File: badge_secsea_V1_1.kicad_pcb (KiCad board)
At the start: 4 copper layers, 74.1 x 130 mm, 132 parts, among them J1 USB_C_Receptacle_USB2.0_14P, J2 PM254-2-06-S-8.5, J3 PM254-2-06-S-8.5, J4 AFC07-S24ECA-00, J5 Micro_SD_Card_Det1, Q1 2N7002, Q2 SI1308EDL, Q3 SI2301, SW1 TS-1187A-B-A-B, SW2 K2-1112SW-A4SW-04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

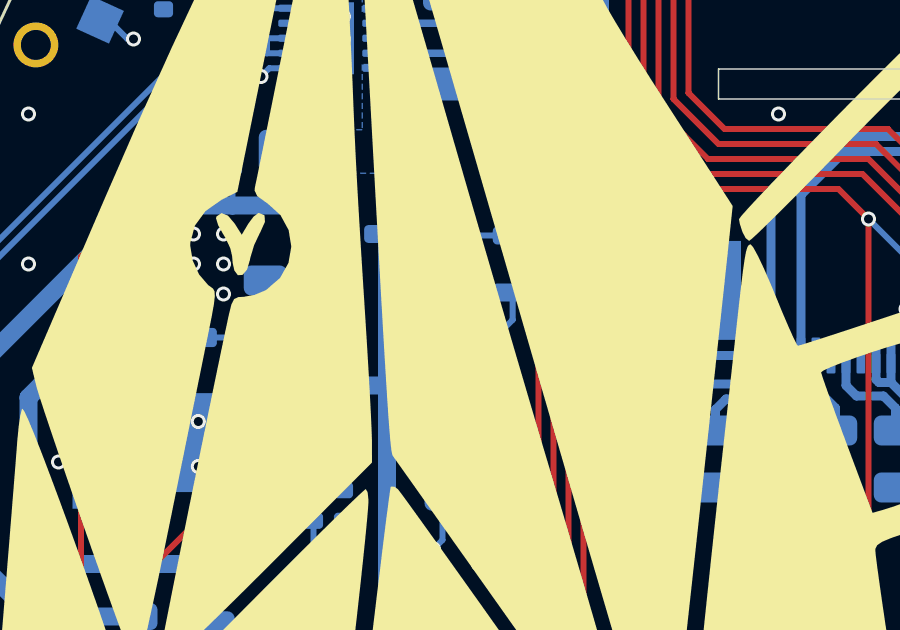
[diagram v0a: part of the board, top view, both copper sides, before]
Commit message: Consumption fix: Op amp now connected to +3.3V instead of VBat (Schematic + PCB)
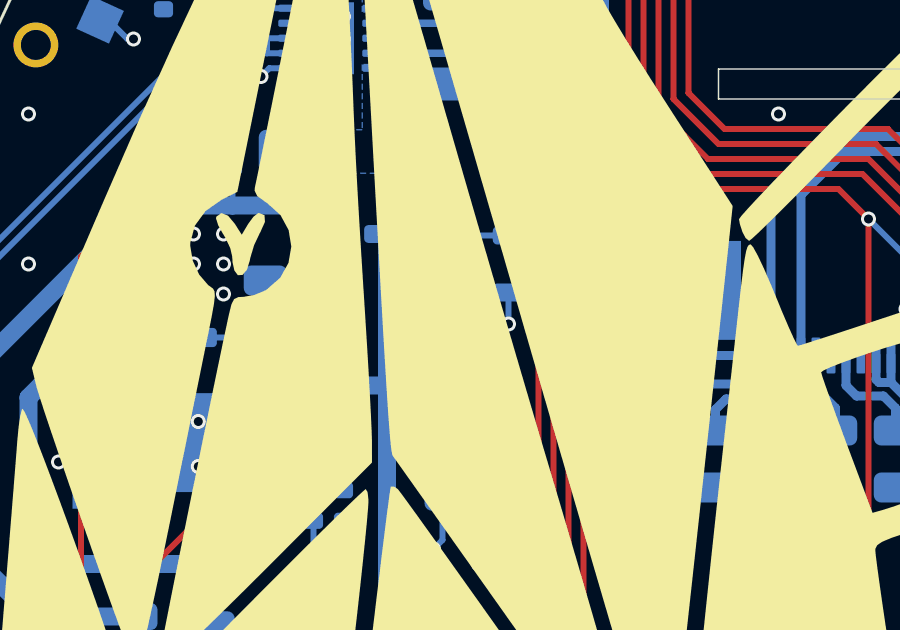
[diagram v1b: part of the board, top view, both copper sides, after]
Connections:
- U7 pad 5: Net-(Q3-D) -> +3.3V
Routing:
- net +3.3V: track 531.5 -> 538.0 mm, vias 38 -> 39
- net Net-(Q3-D): track 47.9 -> 42.6 mm

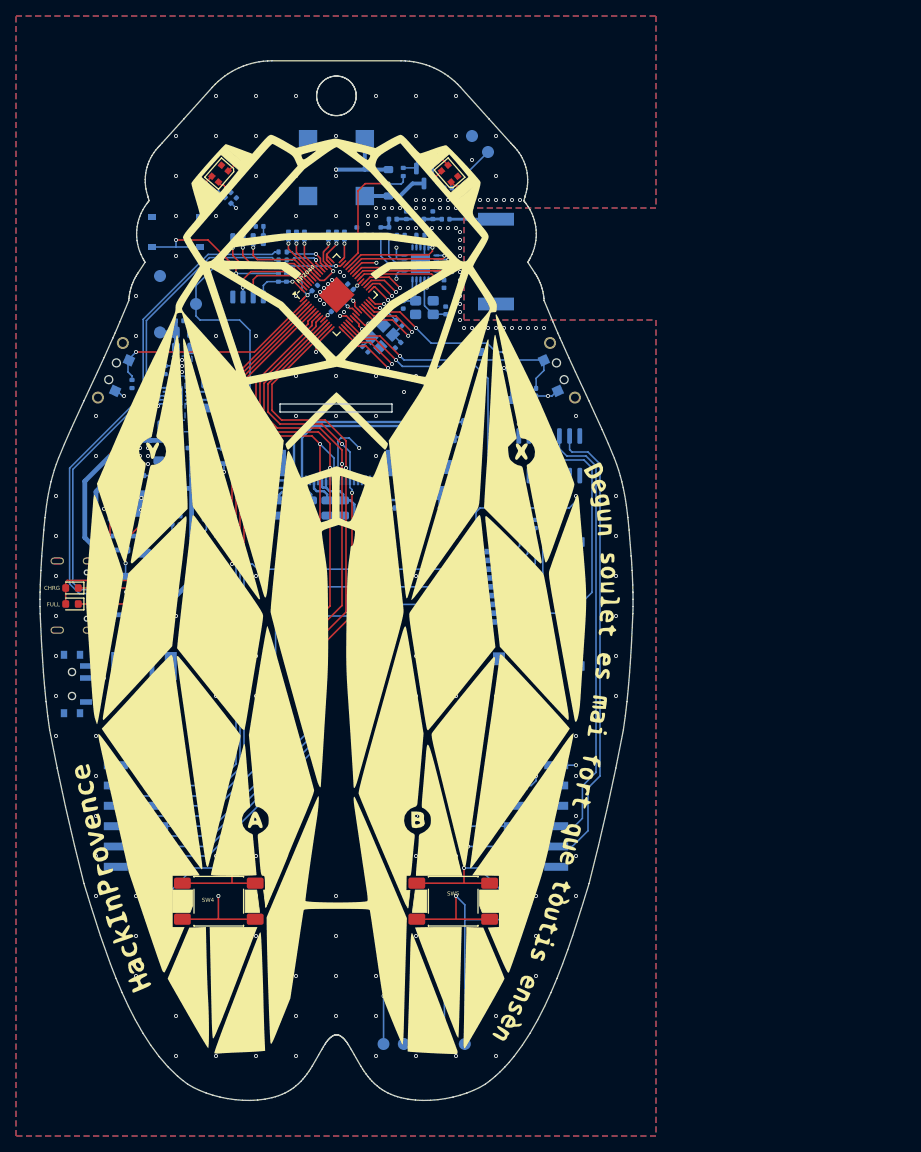
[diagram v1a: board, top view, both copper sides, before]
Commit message: Working on new antenna keepout zone and position.
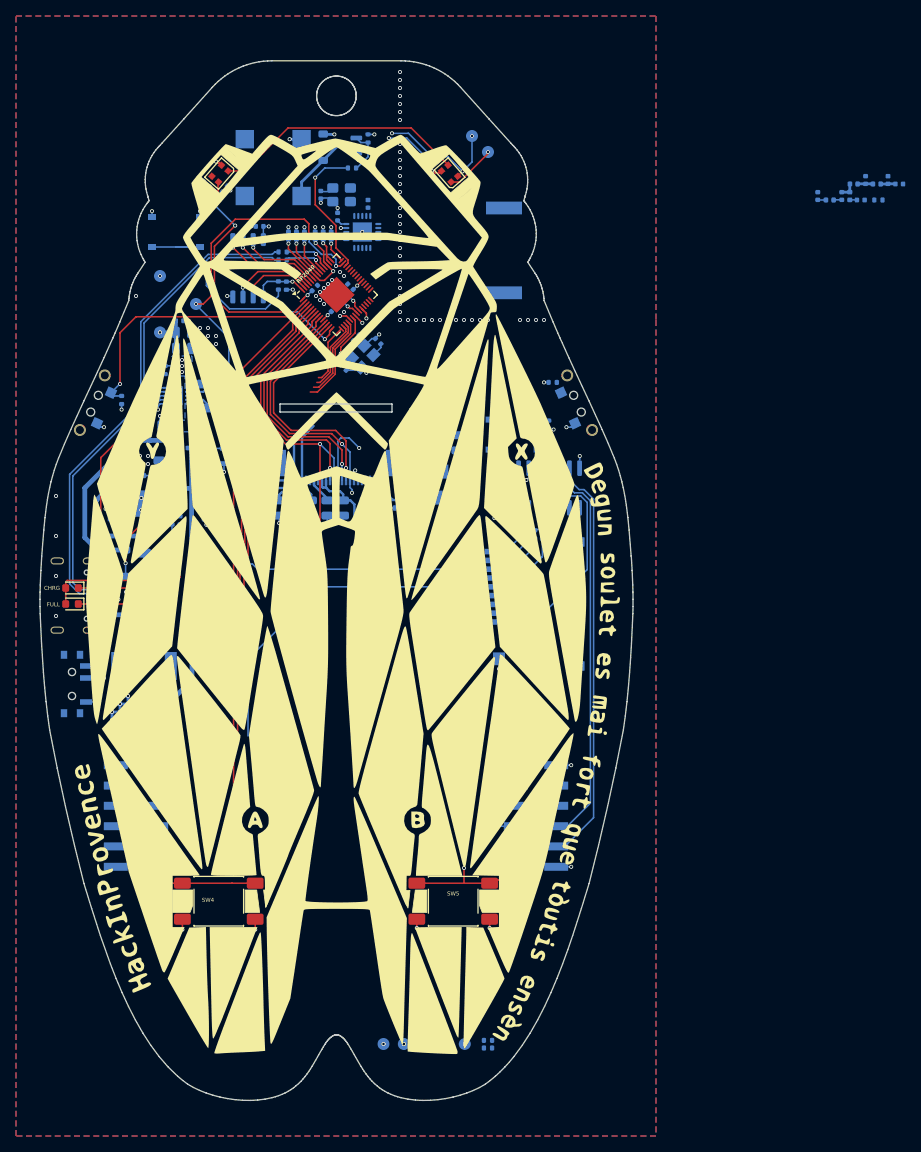
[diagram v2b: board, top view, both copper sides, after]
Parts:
- moved C21 57.8 mm to (160.2, 52.5)
- moved C23 57.8 mm to (163.2, 52.5)
- moved L1 57.8 mm to (164.2, 52.5)
- moved L2 57.8 mm to (161.7, 53.0)
- moved L3 57.8 mm to (164.7, 51.0)
- moved C22 57.7 mm to (165.6, 53.0)
- moved C24 57.6 mm to (166.2, 50.5)
- moved R15 57.4 mm to (167.8, 53.0)
- moved L4 57.3 mm to (167.6, 51.0)
- moved C25 57.1 mm to (169.0, 50.5)
- moved C26 56.9 mm to (170.4, 51.0)
- moved X2 17.5 mm to (100.7, 52.4)
- moved R23 17.5 mm to (119.0, 158.1)
- moved R22 17.5 mm to (119.0, 159.0)
- moved C18 17.2 mm to (98.1, 52.4)
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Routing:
- net +3.3V: track 538.0 -> 93.1 mm, vias 39 -> 47
- net RUN: track 136.4 -> 0.00 mm, vias 4 -> 1
- net Net-(U1-SWD): track 106.3 -> 0.00 mm, vias 3 -> 1
- net Net-(U1-SWCLK): track 107.1 -> 1.74 mm, vias 3 -> 2
- net GND: track 3.71 -> 95.3 mm, vias 287 -> 174
- net SPI0_TX_MOSI: track 132.9 -> 41.5 mm, vias 2 -> 1
- net GPIO14_BUTTON_B: track 102.6 -> 23.9 mm, vias 3 -> 2
- net I2C0_SDA: track 77.6 -> 0.00 mm, vias 2 -> 0
- net I2C0_SCL: track 75.0 -> 0.00 mm, vias 2 -> 0
- net GPIO_20: track 76.1 -> 1.88 mm, vias 2 -> 1
- net UART0_TX: track 81.5 -> 9.38 mm, vias 2 -> 1
- net UART0_RX: track 80.2 -> 11.1 mm, vias 2 -> 1
- net GPIO10_SCREEN_RST: track 95.7 -> 29.1 mm, vias 2 -> 1
- net SD_DETECT: track 67.2 -> 4.25 mm, vias 2 -> 0
- net GPIO8_SCREEN_DC: track 92.0 -> 29.6 mm, vias 2 -> 1
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- removed copper zone on In1.Cu, net GND

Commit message: SAO connector added (with 3D). WIP on the antenna.
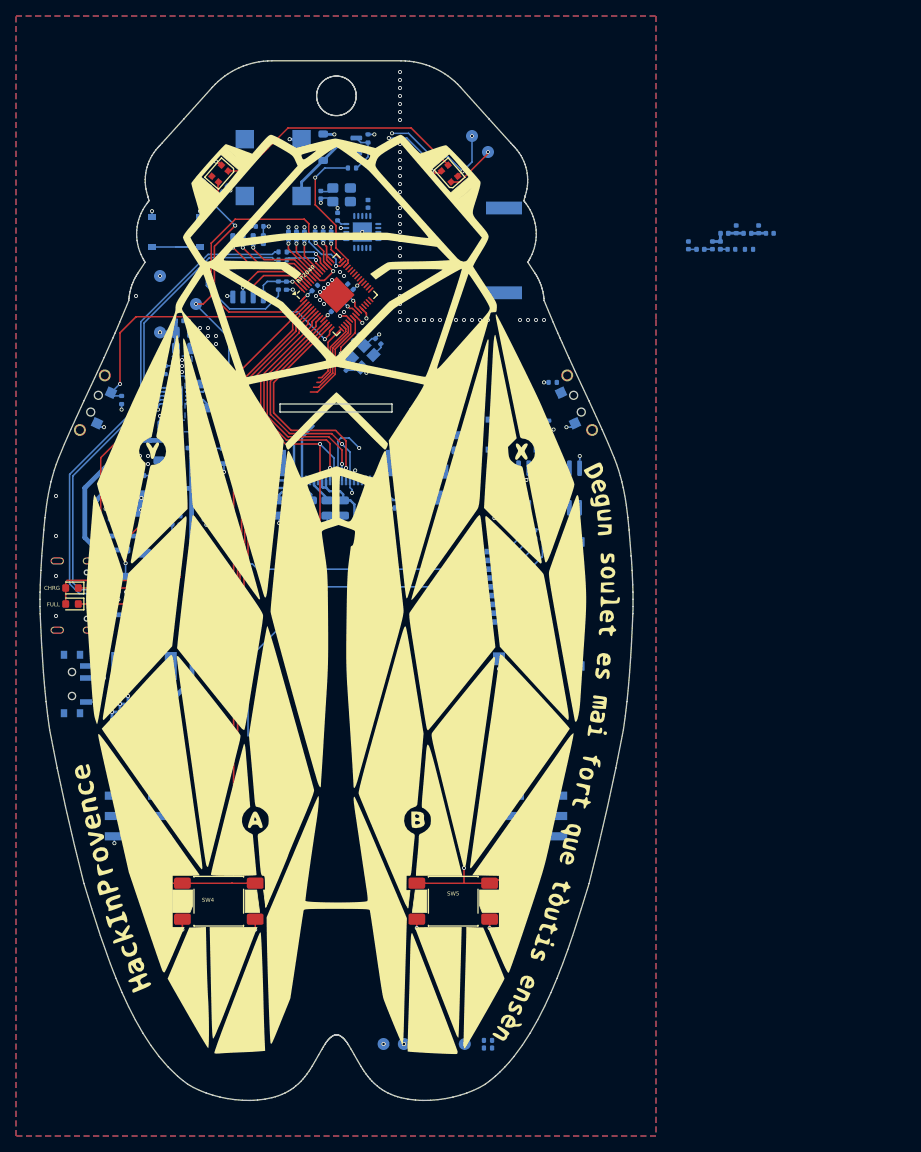
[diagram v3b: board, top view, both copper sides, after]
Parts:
- removed J2, J3: PM254-2-06-S-8.5, Connector_PinSocket_2.54mm:PinSocket_2x06_P2.54mm_Vertical_SMD
- added SAO0: HC-PM254-8.5H-2X3PS, lcsc_footprints:C22373944_HDR-SMD_6P-P2_54-V-F-R2-C3-LS7_1, B.Cu at (75.0, 130.0)
- added SAO1: HC-PM254-8.5H-2X3PS, lcsc_footprints:C22373944_HDR-SMD_6P-P2_54-V-F-R2-C3-LS7_1, B.Cu at (125.0, 130.0)
- moved C21 17.3 mm to (144.0, 58.7)
- moved C22 17.3 mm to (149.4, 59.2)
- moved C23 17.3 mm to (147.0, 58.7)
- moved C24 17.3 mm to (150.0, 56.7)
- moved C25 17.3 mm to (152.8, 56.7)
- moved C26 17.3 mm to (154.2, 57.2)
- moved L1 17.3 mm to (148.0, 58.7)
- moved L2 17.3 mm to (145.5, 59.2)
- moved L3 17.3 mm to (148.5, 57.2)
- moved L4 17.3 mm to (151.4, 57.2)
- moved R15 17.3 mm to (151.6, 59.2)
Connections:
- net SPI0_CS1 renamed SPI0_CS1_SD
- U1 pad 30: GPIO19_SPI0_CS_A1 -> GPIO19
- U2 pad 3: GPIO19_SPI0_CS_A1 -> GND
- U2 pad 6: SPI0_CS2 -> unconnected-(U2A-1Y2-Pad6)
- U2 pad 7: SPI0_CS3 -> unconnected-(U2A-1Y3-Pad7)
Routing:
- net SPI0_CS3: track 51.5 -> 0.00 mm
- net SPI0_CS2: track 49.5 -> 0.00 mm
- net SPI0_CS1_SD: track 30.0 -> 0.00 mm
- net +3.3V: track 93.1 -> 85.4 mm
- net UART0_RX: track 11.1 -> 8.83 mm, vias 1 -> 0
- net UART0_TX: track 9.38 -> 7.50 mm, vias 1 -> 0
- net GPIO_20: track 1.88 -> 0.00 mm, vias 1 -> 0
- net GPIO19_SPI0_CS_A1: track 1.60 -> 0.00 mm, vias 1 -> 0
- net GND: track 95.3 -> 96.3 mm, vias 174 -> 175

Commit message: WIP routing
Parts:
- moved C25 35.2 mm to (119.5, 68.0), turned to 180 degrees
- moved C26 34.8 mm to (121.0, 67.5), turned to -90 degrees
- moved TP6 33.5 mm to (86.4, 39.4)
- moved L4 32.8 mm to (121.0, 69.5), turned to 90 degrees
- moved TP7 32.8 mm to (84.4, 41.4)
- moved R15 32.8 mm to (124.6, 77.7), turned to -90 degrees
- moved C16 32.1 mm to (119.5, 80.7), turned to 180 degrees
- moved C22 31.5 mm to (121.9, 74.4)
- moved L3 31.0 mm to (121.0, 71.5), turned to 90 degrees
- moved C24 31.0 mm to (122.5, 71.0), turned to 0 degrees
- moved C23 30.6 mm to (120.0, 72.9)
- moved C21 29.8 mm to (118.4, 73.9)
- moved L2 29.7 mm to (120.0, 74.4)
- moved L1 29.7 mm to (122.0, 72.9)
- moved U4 27.4 mm to (121.2, 77.7), turned to 90 degrees
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- renumbered L5 to ANT0
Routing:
- net Net-(LED2-DOUT): track 6.29 -> 37.0 mm
- net SPI0_RX_MISO: track 93.3 -> 64.1 mm
- net SPI0_SCK: track 100.9 -> 79.6 mm
- net SPI1_TX_MOSI_RADIO_SI: track 0.00 -> 21.2 mm
- net SPI1_SCK_RADIO: track 0.00 -> 20.9 mm
- net SPI1_CSn_RADIO: track 0.00 -> 20.7 mm
- net SPI1_RX_MISO_RADIO_SO: track 0.00 -> 20.3 mm
- net GPIO23_RADIO_GDO2: track 0.00 -> 20.1 mm
- net GPIO22_RADIO_GDO0: track 0.00 -> 19.5 mm
- net GPIO18_SPI0_CS_A0: track 1.57 -> 19.9 mm
- net I2C0_SCL: track 0.00 -> 16.5 mm
- net SD_DETECT: track 4.25 -> 11.4 mm
- net GPIO_20: track 0.00 -> 6.39 mm
- net GPIO19: track 0.00 -> 5.48 mm
- net GPIO15_BUTTON_X: track 11.4 -> 8.56 mm
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
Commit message: WIP Routing....
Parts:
- moved SAO0 50.0 mm to (125.0, 130.0), turned to -90 degrees
- moved SAO1 50.0 mm to (75.0, 130.0)
- moved C18 3.95 mm to (116.0, 75.2), turned to 180 degrees
- moved C44 3.69 mm to (118.0, 109.1)
- moved C11 3.38 mm to (104.1, 74.5), turned to 45 degrees
- moved C17 3.15 mm to (116.6, 80.5), turned to 0 degrees
- moved D3 2.82 mm to (109.5, 80.7)
- moved D4 2.82 mm to (109.5, 78.2)
- moved SW1 2.60 mm to (124.8, 87.1)
- moved X2 2.55 mm to (116.2, 77.8), turned to 90 degrees
- moved C27 2.11 mm to (115.0, 86.0)
- moved R17 1.67 mm to (108.2, 92.8), turned to 0 degrees
- moved C29 1.30 mm to (96.2, 91.5)
- moved C31 1.30 mm to (102.2, 91.5)
- moved C32 1.30 mm to (100.2, 91.5)
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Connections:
- SAO0 pad 5: UART0_RX -> GPIO19
- SAO0 pad 6: UART0_TX -> GPIO_20
- SAO1 pad 5: GPIO19 -> UART0_RX
- SAO1 pad 6: GPIO_20 -> UART0_TX
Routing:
- net RUN: track 0.00 -> 106.7 mm, vias 1 -> 2
- net UART0_TX: track 6.98 -> 91.3 mm, vias 0 -> 3
- net Net-(U1-SWD): track 0.00 -> 80.0 mm, vias 1 -> 2
- net GPIO19: track 5.48 -> 85.5 mm, vias 0 -> 1
- net UART0_RX: track 7.42 -> 82.8 mm, vias 0 -> 3
- net GPIO_20: track 6.39 -> 79.2 mm, vias 0 -> 1
- net Net-(U1-SWCLK): track 1.74 -> 67.2 mm, vias 2 -> 3
- net I2C0_SCL: track 16.5 -> 80.8 mm, vias 0 -> 1
- net GPIO14_BUTTON_B: track 21.9 -> 66.2 mm
- net SD_DETECT: track 11.4 -> 50.5 mm, vias 0 -> 1
- net I2C1_SCL: track 55.5 -> 82.4 mm, vias 0 -> 1
- net GPIO18_SPI0_CS_A0: track 19.9 -> 42.7 mm, vias 1 -> 2
- net SPI0_CS1_SD: track 0.00 -> 21.9 mm
- net SPI1_TX_MOSI_RADIO_SI: track 21.2 -> 40.4 mm, vias 0 -> 3
- net I2C1_SDA: track 57.3 -> 75.5 mm, vias 0 -> 1
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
